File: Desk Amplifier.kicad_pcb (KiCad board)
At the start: 2 copper layers, 110 x 75.3 mm, 29 parts, among them J1 AudioJack3, J2 AudioJack3, J3 AudioJack3, J4 AudioJack3, J5 Barrel_Jack, U1 OPA2134, U2 OPA2134

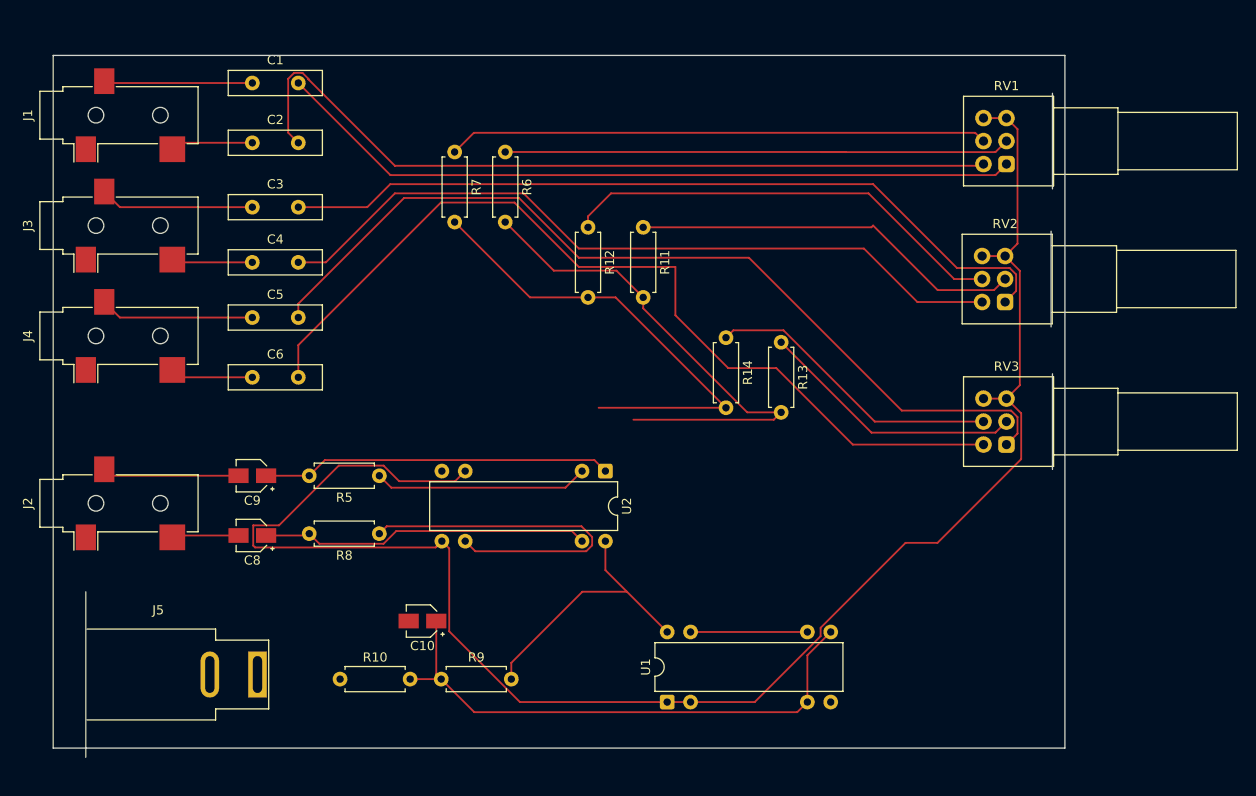
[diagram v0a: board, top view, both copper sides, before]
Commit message: updated with real components
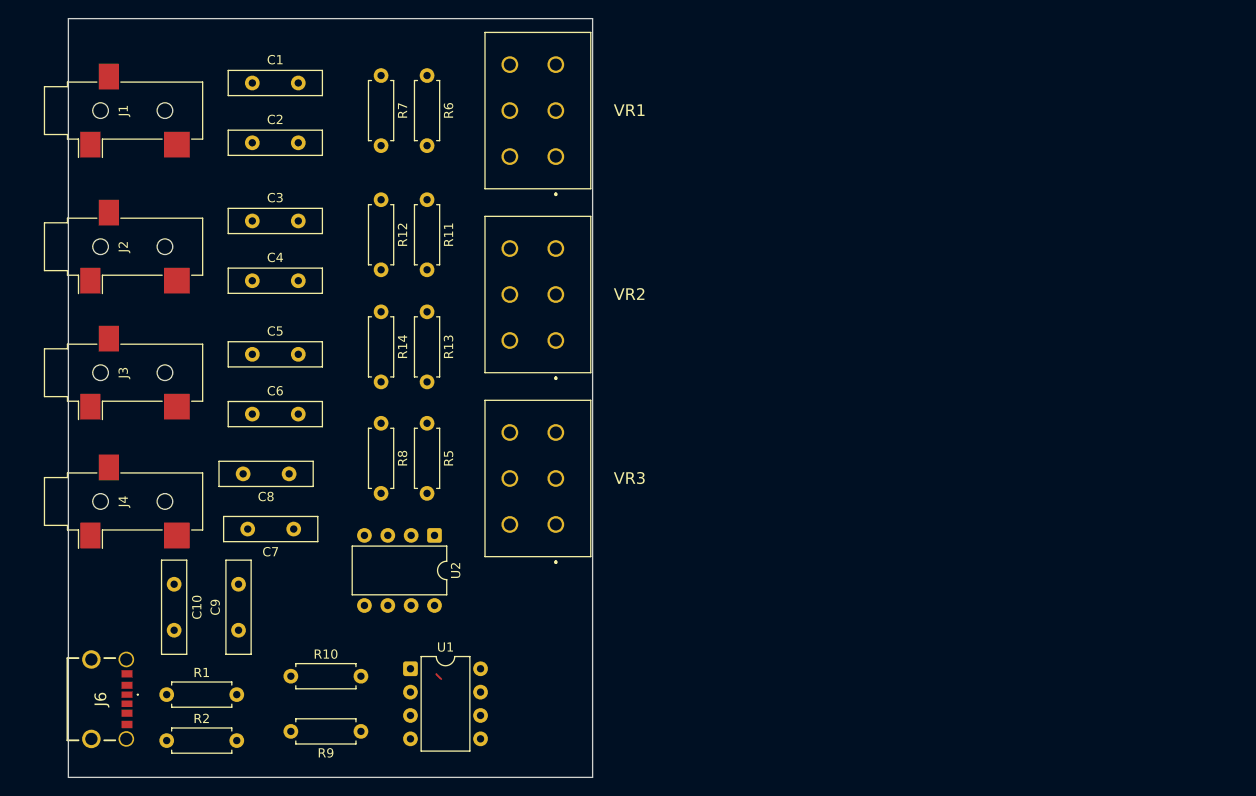
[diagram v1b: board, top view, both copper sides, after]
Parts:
- removed the J4 at (86.0, 90.5)
- removed J5: Barrel_Jack, Connector_BarrelJack:BarrelJack_SwitchcraftConxall_RAPC10U_Horizontal
- removed RV1, RV2, RV3: R_Potentiometer_Dual, Potentiometer_THT:Potentiometer_Alps_RK097_Dual_Horizontal
- added C7: 10uF, Capacitor_THT:C_Disc_D10.0mm_W2.5mm_P5.00mm, F.Cu at (105.0, 111.5)
- added J2: AudioJack3, Connector_Audio:Jack_3.5mm_CUI_SJ-3523-SMT_Horizontal, F.Cu at (86.5, 80.8)
- added J6: USB4970-00-A, Footprint Library:USB497000A, F.Cu at (83.0, 130.0)
- added R1: 5.1k, Resistor_THT:R_Axial_DIN0207_L6.3mm_D2.5mm_P7.62mm_Horizontal, F.Cu at (91.2, 129.5)
- added R2: 5.1k, Resistor_THT:R_Axial_DIN0207_L6.3mm_D2.5mm_P7.62mm_Horizontal, F.Cu at (91.2, 134.5)
- added VR1: PDB182-K420K-103A2, Footprint Library:PDB182K420P204A2, F.Cu at (133.5, 71.0)
- added VR2: PDB182-K420K-103A2, Footprint Library:PDB182K420P204A2, F.Cu at (133.5, 91.0)
- added VR3: PDB182-K420K-103A2, Footprint Library:PDB182K420P204A2, F.Cu at (133.5, 111.0)
- C10, C9: value C_Polarized -> 100pF; footprint Capacitor_SMD:CP_Elec_3x5.3 -> Capacitor_THT:C_Disc_D10.0mm_W2.5mm_P5.00mm
- C8: value C_Polarized -> 10uF; footprint Capacitor_SMD:CP_Elec_3x5.3 -> Capacitor_THT:C_Disc_D10.0mm_W2.5mm_P5.00mm
- U1, U2: footprint Package_DIP:DIP-8-16_W7.62mm -> Package_DIP:DIP-8_W7.62mm
- moved R13 38.6 mm to (119.5, 87.9)
- moved R14 37.6 mm to (114.5, 87.9)
- moved U1 28.1 mm to (117.7, 126.7), turned to 0 degrees
- moved C10 27.3 mm to (92.0, 117.5), turned to -90 degrees
- moved R11 23.7 mm to (119.5, 75.7)
- moved R12 22.7 mm to (114.5, 75.7)
- moved U2 19.9 mm to (120.3, 112.2)
- moved C9 16.9 mm to (99.0, 122.5), turned to 90 degrees
- moved J3 16.0 mm to (86.5, 94.5)
- moved R8 12.0 mm to (114.5, 100.0), turned to -90 degrees
- moved R6 11.9 mm to (119.5, 62.2)
- moved R7 11.5 mm to (114.5, 62.2)
- moved R9 10.4 mm to (112.3, 133.5), turned to 180 degrees
- moved C8 7.80 mm to (104.5, 105.5)
- moved R5 7.71 mm to (119.5, 100.0), turned to -90 degrees
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- renumbered J2 to J4
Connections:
- C10 pad 1: Net-(U1A-+) -> GND
- C10 pad 2: GND -> +5V
- C9 pad 1: Net-(C9-Pad1) -> GND
- C9 pad 2: Net-(C9-Pad2) -> /Vbias
- J3 pad R: Net-(C3-Pad1) -> Net-(C5-Pad1)
- J3 pad T: Net-(C4-Pad1) -> Net-(C6-Pad1)
- J4 pad R: Net-(C9-Pad2) -> Net-(C8-Pad2)
- J4 pad T: Net-(C8-Pad2) -> Net-(C7-Pad2)
- R5 pad 2: Net-(C9-Pad1) -> Net-(C8-Pad1)
- R8 pad 2: Net-(C8-Pad1) -> Net-(C7-Pad1)
- U2 pad 1: Net-(C9-Pad1) -> Net-(C8-Pad1)
- U2 pad 7: Net-(C8-Pad1) -> Net-(C7-Pad1)
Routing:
- net /Vbias: track 184.5 -> 0.00 mm
- net Net-(C6-Pad2): track 98.4 -> 0.00 mm
- net Net-(C5-Pad2): track 97.8 -> 0.00 mm
- net Net-(U2B--): track 91.1 -> 0.00 mm
- net Net-(C2-Pad2): track 87.6 -> 0.00 mm
- net Net-(C3-Pad2): track 86.6 -> 0.00 mm
- net Net-(C4-Pad2): track 82.4 -> 0.00 mm
- net Net-(C1-Pad2): track 81.6 -> 0.00 mm
- net Net-(U2A--): track 79.0 -> 0.00 mm
- net Net-(U1A-+): track 60.3 -> 0.76 mm
- net Net-(R7-Pad1): track 58.7 -> 0.00 mm
- net Net-(R6-Pad1): track 57.7 -> 0.00 mm
- net Net-(R12-Pad1): track 48.9 -> 0.00 mm
- net Net-(R11-Pad1): track 42.8 -> 0.00 mm
- net Net-(C9-Pad1): track 38.1 -> 0.00 mm
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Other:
- board size 110 x 75.3 mm -> 57 x 82.5 mm

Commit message: use STX-3000 for 2.5mm jack connection + routing
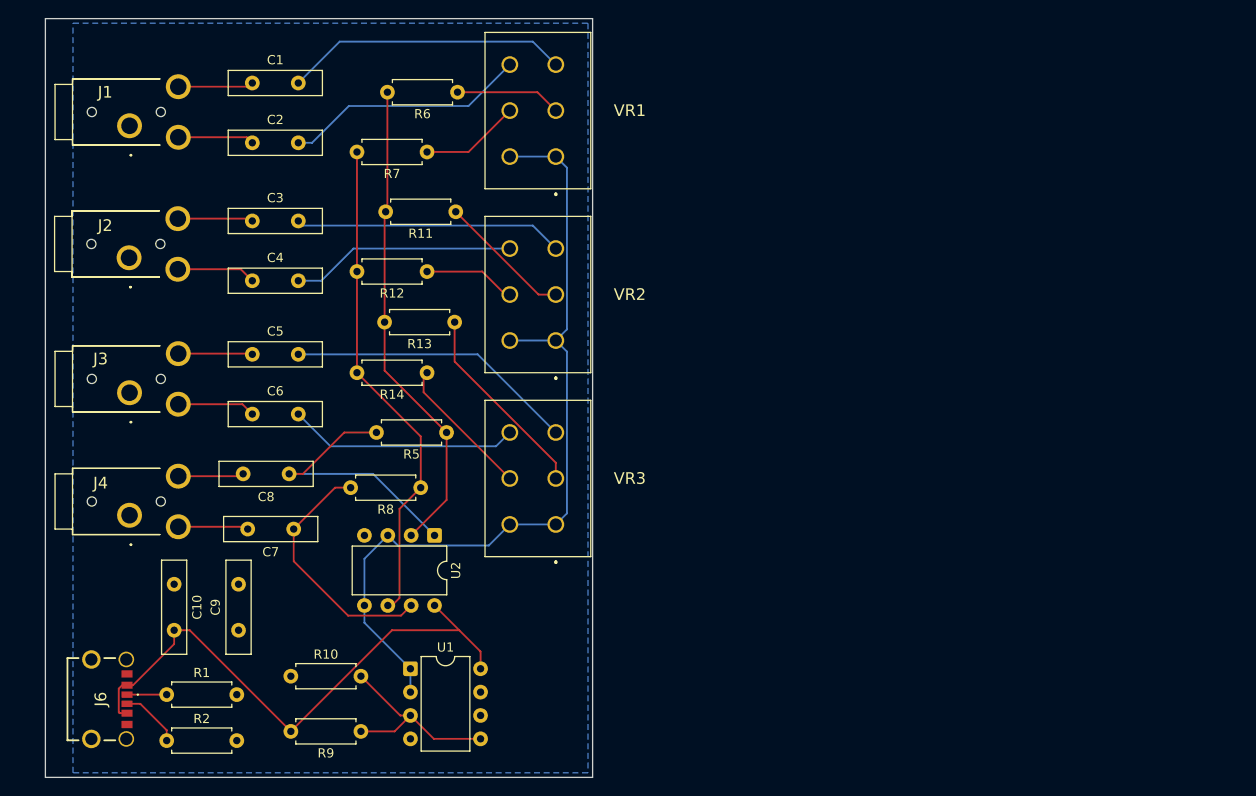
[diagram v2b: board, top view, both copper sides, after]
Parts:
- J1, J2, J3, J4: value AudioJack3 -> STX-3000; footprint Connector_Audio:Jack_3.5mm_CUI_SJ-3523-SMT_Horizontal -> Footprint Library:STX3000
- moved R7 9.70 mm to (119.5, 70.5), turned to 180 degrees
- moved R12 9.27 mm to (119.5, 83.5), turned to 180 degrees
- moved R14 8.30 mm to (119.5, 94.5), turned to 180 degrees
- moved R8 8.22 mm to (118.8, 107.0), turned to 180 degrees
- moved R6 3.77 mm to (122.8, 64.0), turned to 180 degrees
- moved R11 3.38 mm to (122.6, 77.0), turned to 180 degrees
- moved R13 3.20 mm to (122.5, 89.0), turned to 180 degrees
- moved R5 2.34 mm to (121.6, 101.0), turned to 180 degrees
- moved J3 2.27 mm to (87.2, 96.7), turned to 0 degrees
- moved J1 1.78 mm to (87.2, 67.7), turned to 0 degrees
- moved J4 1.63 mm to (87.2, 110.0), turned to 0 degrees
- moved J2 1.34 mm to (87.1, 82.0), turned to 0 degrees
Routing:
- net /Vbias: track 0.00 -> 91.8 mm
- net +5V: track 0.00 -> 62.1 mm
- net Net-(U2B--): track 0.00 -> 53.9 mm
- net Net-(U2A--): track 0.00 -> 52.7 mm
- net Net-(C5-Pad2): track 0.00 -> 31.5 mm
- net Net-(C1-Pad2): track 0.00 -> 30.9 mm
- net Net-(C8-Pad1): track 0.00 -> 29.9 mm
- net Net-(C3-Pad2): track 0.00 -> 29.2 mm
- net Net-(C7-Pad1): track 0.00 -> 27.2 mm
- net Net-(C2-Pad2): track 0.00 -> 26.5 mm
- net Net-(C6-Pad2): track 0.00 -> 25.1 mm
- net Net-(C4-Pad2): track 0.00 -> 24.4 mm
- net Net-(R13-Pad1): track 0.00 -> 21.6 mm
- net Net-(U1A-+): track 0.76 -> 21.9 mm
- net Net-(R14-Pad1): track 0.00 -> 15.4 mm
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- added copper zone on B.Cu, net GND
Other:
- board size 57 x 82.5 mm -> 59.5 x 82.5 mm

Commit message: add vbias plane on f.cu, update j1-4 to protrude over edge
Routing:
- net /Vbias: track 91.8 -> 2.54 mm
- added copper zone on F.Cu, net /Vbias
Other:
- board size 59.5 x 82.5 mm -> 57 x 82.5 mm

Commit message: update routing, add name
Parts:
- added H1: MountingHole, MountingHole:MountingHole_2.1mm, F.Cu at (131.5, 131.5)
- added H2: MountingHole, MountingHole:MountingHole_2.1mm, F.Cu at (111.5, 62.5)
- added H3: MountingHole, MountingHole:MountingHole_2.1mm, F.Cu at (86.5, 119.0)
- moved C10 8.84 mm to (98.0, 124.0), turned to 180 degrees
- moved C9 6.18 mm to (105.0, 124.0), turned to 0 degrees
- moved R10 6.06 mm to (103.9, 133.5)
- moved R9 5.07 mm to (111.5, 128.5)
- moved R6 2.55 mm to (122.3, 66.5)
- moved J4 1.18 mm to (87.2, 111.2)
- moved J6 1.12 mm to (83.5, 129.0)
- moved R1 1.02 mm to (91.4, 128.5)
- moved R2 1.02 mm to (91.4, 133.5)
- moved U1 1.00 mm to (117.7, 125.7)
- moved C8 1.00 mm to (105.5, 105.5)
- moved R7 1.00 mm to (119.5, 71.5)
- moved C7 0.50 mm to (105.5, 111.5)
- moved R11 0.50 mm to (122.6, 77.5)
- moved J2 0.18 mm to (87.1, 82.2)
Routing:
- net +5V: track 62.1 -> 52.5 mm
- net /Vbias: track 2.54 -> 10.9 mm
- net GND: track 0.00 -> 3.21 mm
- net Net-(U1B--): track 0.00 -> 2.54 mm
- net Net-(C8-Pad1): track 29.9 -> 27.4 mm
- net Net-(C3-Pad2): track 29.2 -> 31.7 mm
- net Net-(R6-Pad1): track 11.5 -> 13.5 mm
- net Net-(U2A--): track 52.7 -> 51.0 mm
- net Net-(R11-Pad1): track 14.6 -> 16.1 mm
- net Net-(U1A-+): track 21.9 -> 23.4 mm
- net Net-(C8-Pad2): track 7.15 -> 8.64 mm
- net Net-(C2-Pad2): track 26.5 -> 27.9 mm
- net Net-(U2B--): track 53.9 -> 52.9 mm
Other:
- board size 57 x 82.5 mm -> 57 x 81 mm
- board text added: "Desk Amp Rev 1 Micah Raney micahraney.com 2026"

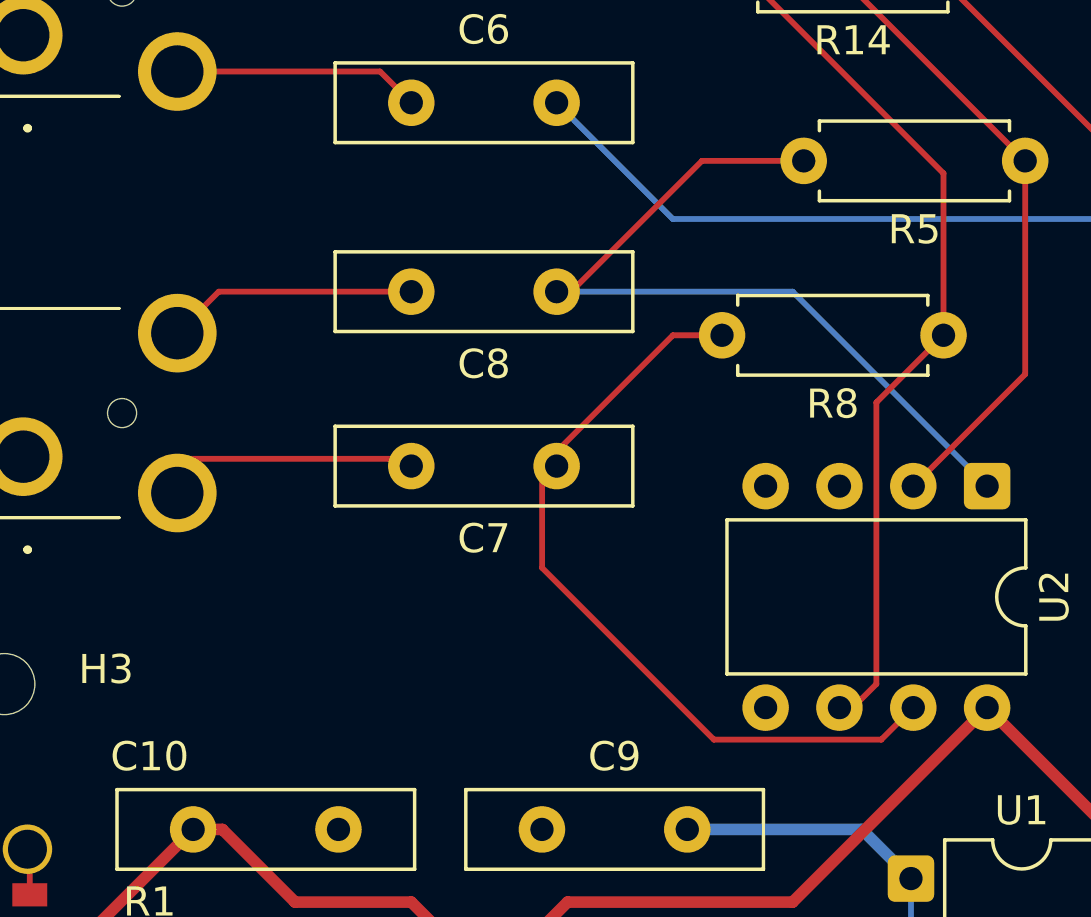
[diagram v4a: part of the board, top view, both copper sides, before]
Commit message: add pull-down caps to output
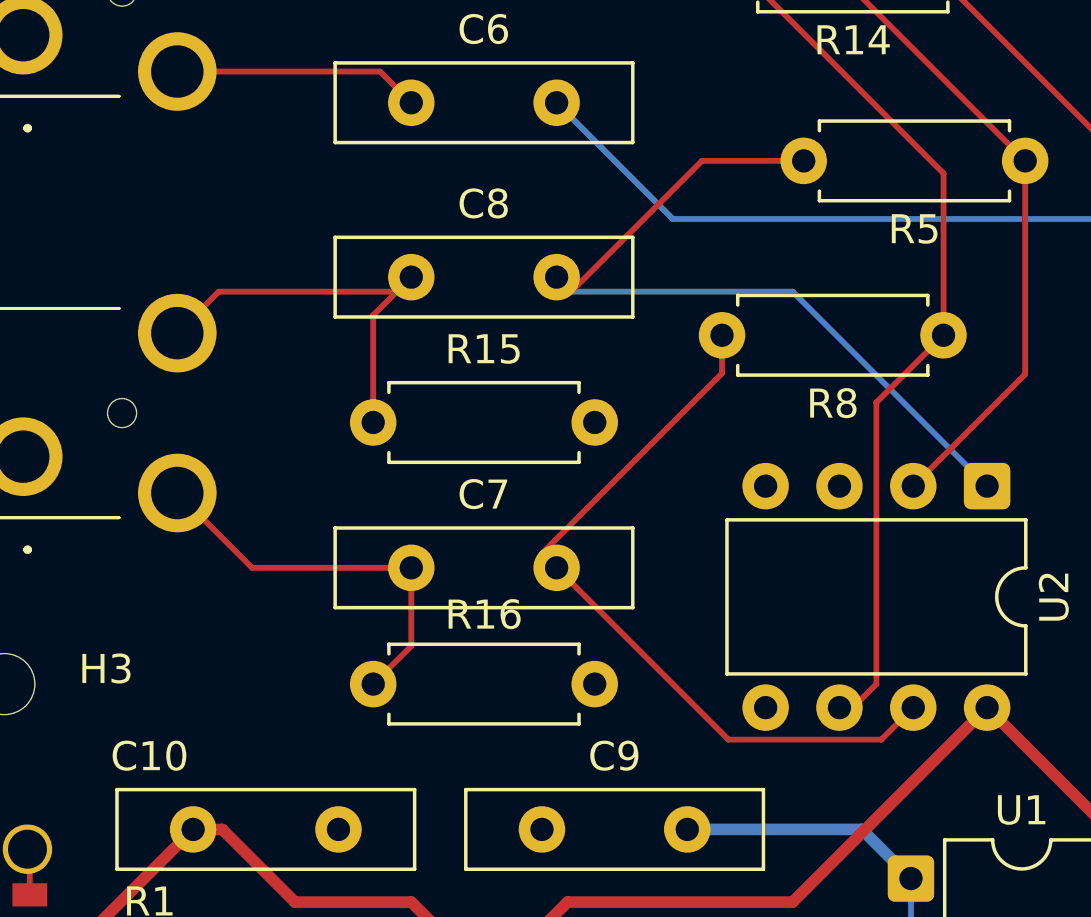
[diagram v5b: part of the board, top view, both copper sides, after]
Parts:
- added R15: 1M, Resistor_THT:R_Axial_DIN0207_L6.3mm_D2.5mm_P7.62mm_Horizontal, F.Cu at (106.8, 110.0)
- added R16: 1M, Resistor_THT:R_Axial_DIN0207_L6.3mm_D2.5mm_P7.62mm_Horizontal, F.Cu at (99.2, 119.0)
- moved C7 3.50 mm to (105.5, 115.0)
- moved C8 0.50 mm to (105.5, 105.0)
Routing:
- net Net-(C7-Pad2): track 7.94 -> 13.9 mm
- net Net-(C8-Pad2): track 8.64 -> 14.2 mm
- net Net-(C7-Pad1): track 27.2 -> 25.9 mm

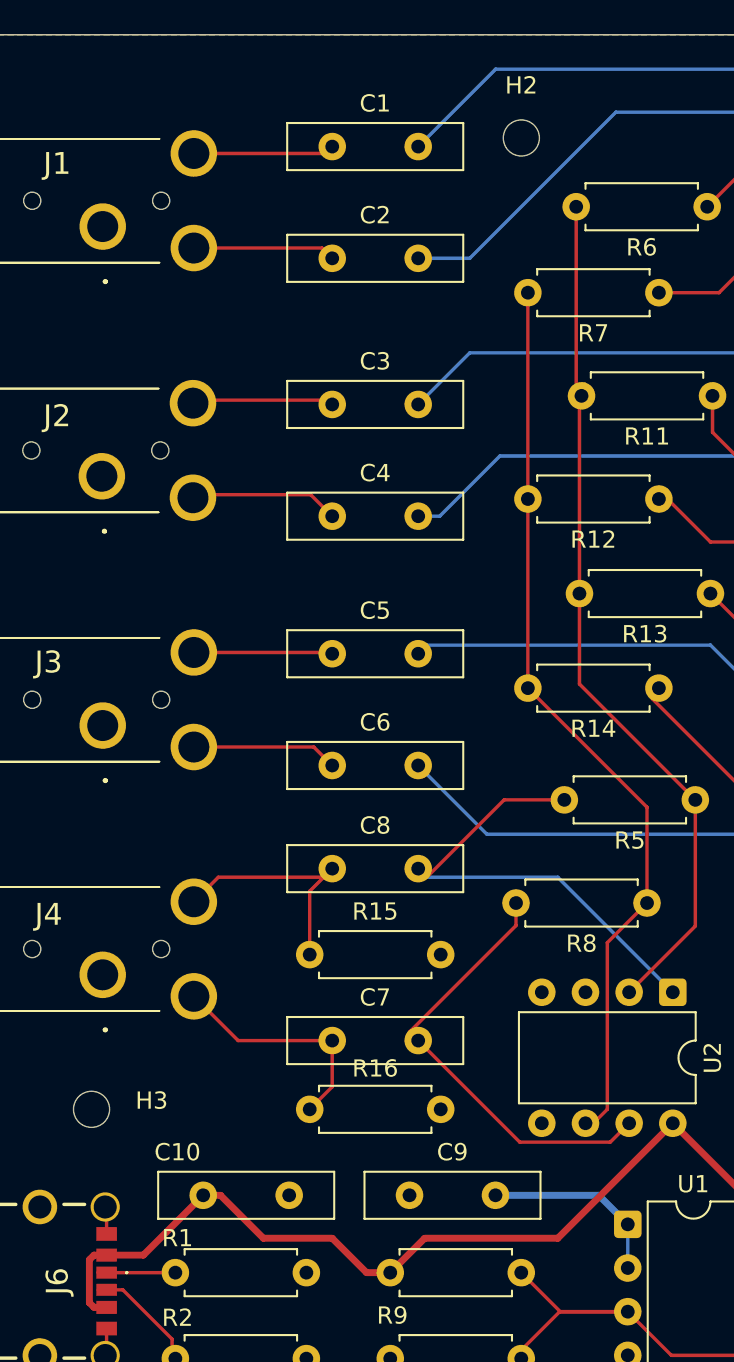
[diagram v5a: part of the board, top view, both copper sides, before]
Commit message: update caps to correct 2.5mm pitch footprint
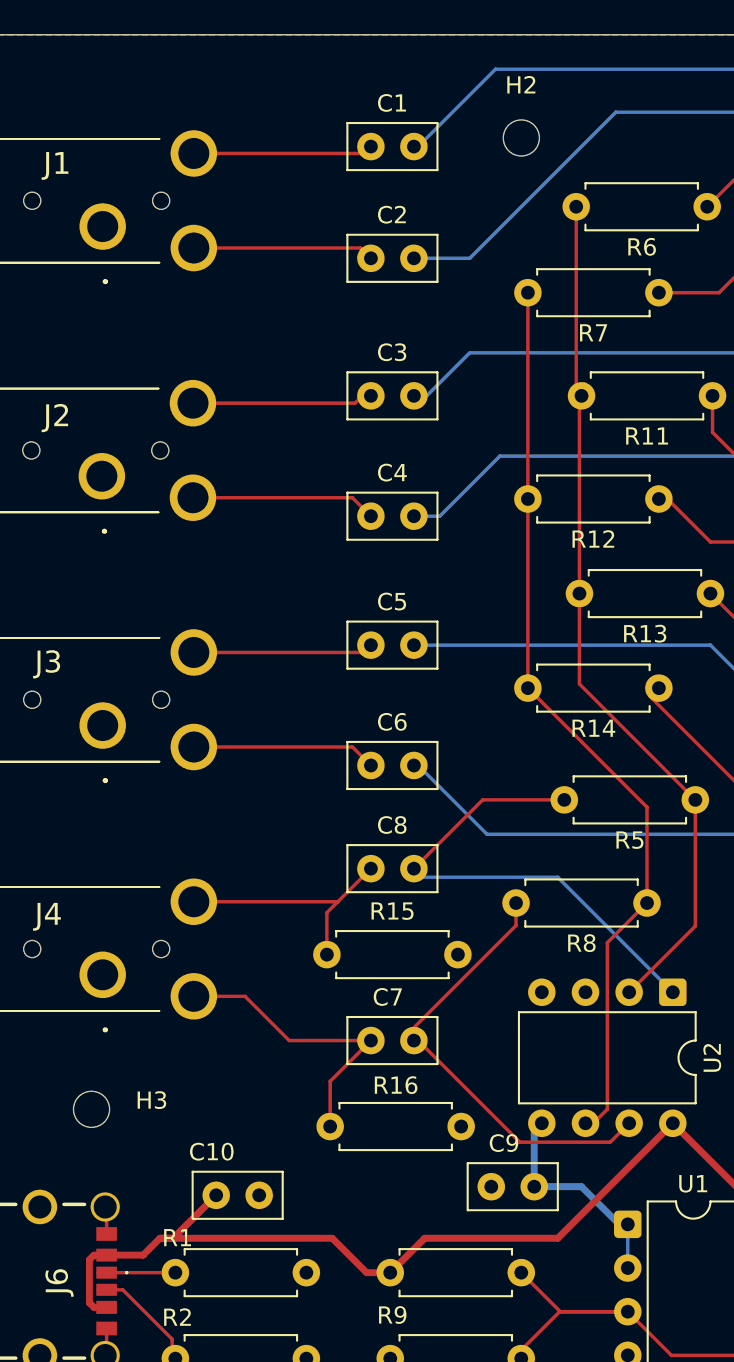
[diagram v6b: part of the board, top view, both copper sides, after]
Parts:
- C1, C10, C2, C3, C4, C5, C6, C7, C8, C9: footprint Capacitor_THT:C_Disc_D10.0mm_W2.5mm_P5.00mm -> Capacitor_THT:C_Disc_D5.0mm_W2.5mm_P2.50mm
- moved C9 4.78 mm to (109.8, 123.5)
- moved C3 2.30 mm to (102.8, 77.5)
- moved C5 2.30 mm to (102.8, 92.0)
- moved C1 2.25 mm to (102.8, 63.0)
- moved C2 2.25 mm to (102.8, 69.5)
- moved C4 2.25 mm to (102.8, 84.5)
- moved C6 2.25 mm to (102.8, 99.0)
- moved C10 1.75 mm to (96.2, 124.0)
- moved R16 1.55 mm to (100.4, 120.0)
- moved R15 1.00 mm to (107.8, 110.0)
- moved C7 0.25 mm to (105.2, 115.0)
- moved C8 0.25 mm to (105.2, 105.0)
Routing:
- net Net-(C7-Pad2): track 13.9 -> 17.3 mm
- net Net-(C3-Pad1): track 8.20 -> 10.7 mm
- net Net-(C5-Pad1): track 8.08 -> 10.6 mm
- net Net-(C6-Pad1): track 8.49 -> 10.7 mm
- net Net-(C2-Pad1): track 8.30 -> 10.5 mm
- net Net-(C1-Pad1): track 8.22 -> 10.5 mm
- net +5V: track 52.5 -> 54.7 mm
- net Net-(C4-Pad1): track 8.62 -> 10.8 mm
- net /Vbias: track 10.9 -> 12.8 mm
- net Net-(C8-Pad1): track 27.4 -> 28.0 mm
